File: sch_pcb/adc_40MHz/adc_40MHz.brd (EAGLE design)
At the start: 100 x 70 mm, 74 parts, among them IC1 AD9235BC, IC2 LT6600-15, IC3 LTC6254XMS, IC4 SN74LVC2G14DBV, IC5 LT1521XST, IC6 SN74LVC2G14DBV, X1 SMA-142-0701-851/861, X2 SMA-142-0701-851/861

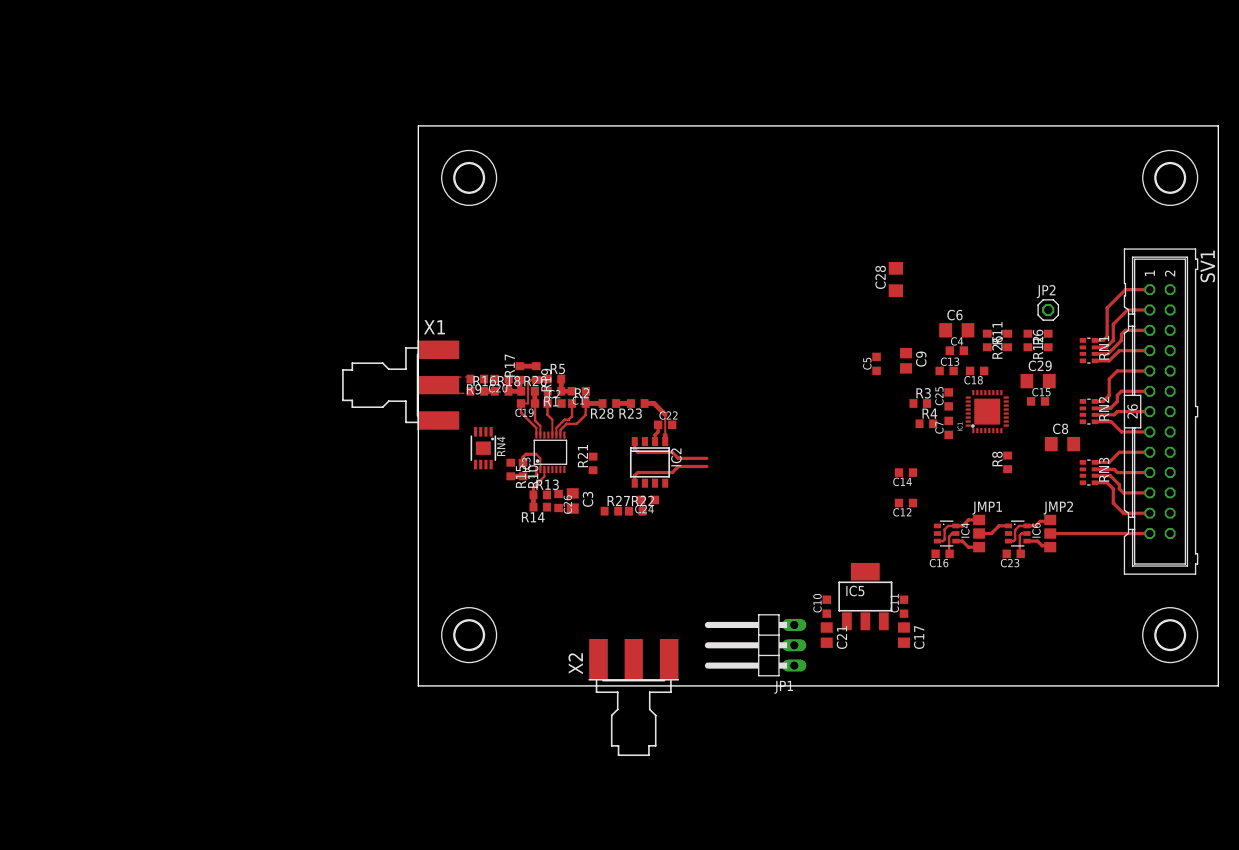
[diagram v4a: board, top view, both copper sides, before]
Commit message: Dodano rezystory ustalające stan buforów. Sygnały w filrach skończone
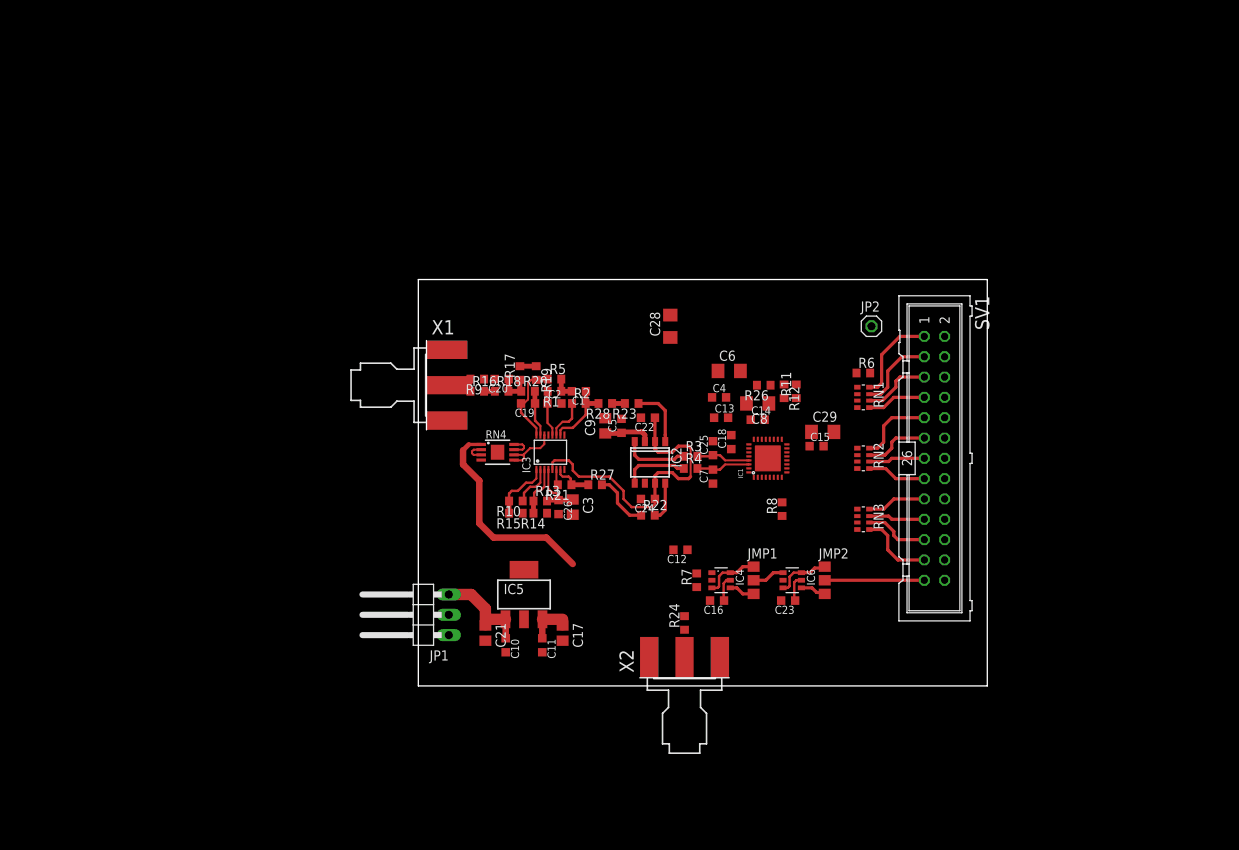
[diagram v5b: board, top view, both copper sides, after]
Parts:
- removed H1, H2, H3, H4: MOUNT-HOLE3.6, holes:3,6
- added R24: 0R, rcl:R0603
- added R7: 1M, rcl:R0603
- moved C11 45.5 mm to (15.5, 5.08), turned to 270 degrees
- moved JP1 43.3 mm to (0.00, 8.89)
- moved C17 42.7 mm to (18.0, 6.60)
- moved C21 42.7 mm to (8.38, 6.60)
- moved IC5 42.7 mm to (13.2, 11.4)
- moved C10 40.4 mm to (10.9, 5.08), turned to 270 degrees
- moved C9 38.5 mm to (23.4, 32.5), turned to 90 degrees
- moved C8 38.4 mm to (42.4, 35.3), turned to 180 degrees
- moved C5 32.8 mm to (25.4, 32.5)
- moved C18 32.0 mm to (39.1, 30.5), turned to 90 degrees
- moved R12 31.1 mm to (45.7, 36.8)
- moved C4 30.3 mm to (37.6, 36.1)
- moved C7 30.1 mm to (36.8, 26.2)
- moved C25 30.1 mm to (36.8, 29.7)
- moved R4 30.0 mm to (34.0, 27.2)
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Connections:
- new net N$18: R24.1, X2.1
- new net SIGIN: R16.1, R9.2, X1.1
- net GND: now also R7.1
- net N$34: now also R24.2, R7.2; no longer X2.1
- net VIN: no longer R16.1, R9.2, X1.1
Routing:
- net +3V3: track 6.51 -> 53.1 mm
- net N$10: track 2.26 -> 38.7 mm
- net VIN: track 0.00 -> 12.4 mm
- net N$24: track 0.00 -> 7.42 mm
- net N$42: track 0.00 -> 7.23 mm
- net N$3: track 0.00 -> 6.76 mm
- net N$2: track 0.00 -> 6.76 mm
- net N$13: track 0.00 -> 5.04 mm
- net N$30: track 0.00 -> 4.94 mm
- net SIGIN: track 0.00 -> 4.80 mm
- net N$15: track 3.95 -> 7.78 mm
- net N$16: track 0.00 -> 2.92 mm
- net N$25: track 0.00 -> 2.70 mm
- net N$1: track 10.4 -> 8.21 mm
- net N$4: track 10.4 -> 8.21 mm
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- removed copper zone on layer 1, net VIN
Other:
- board size 100 x 70 mm -> 71.1 x 50.8 mm

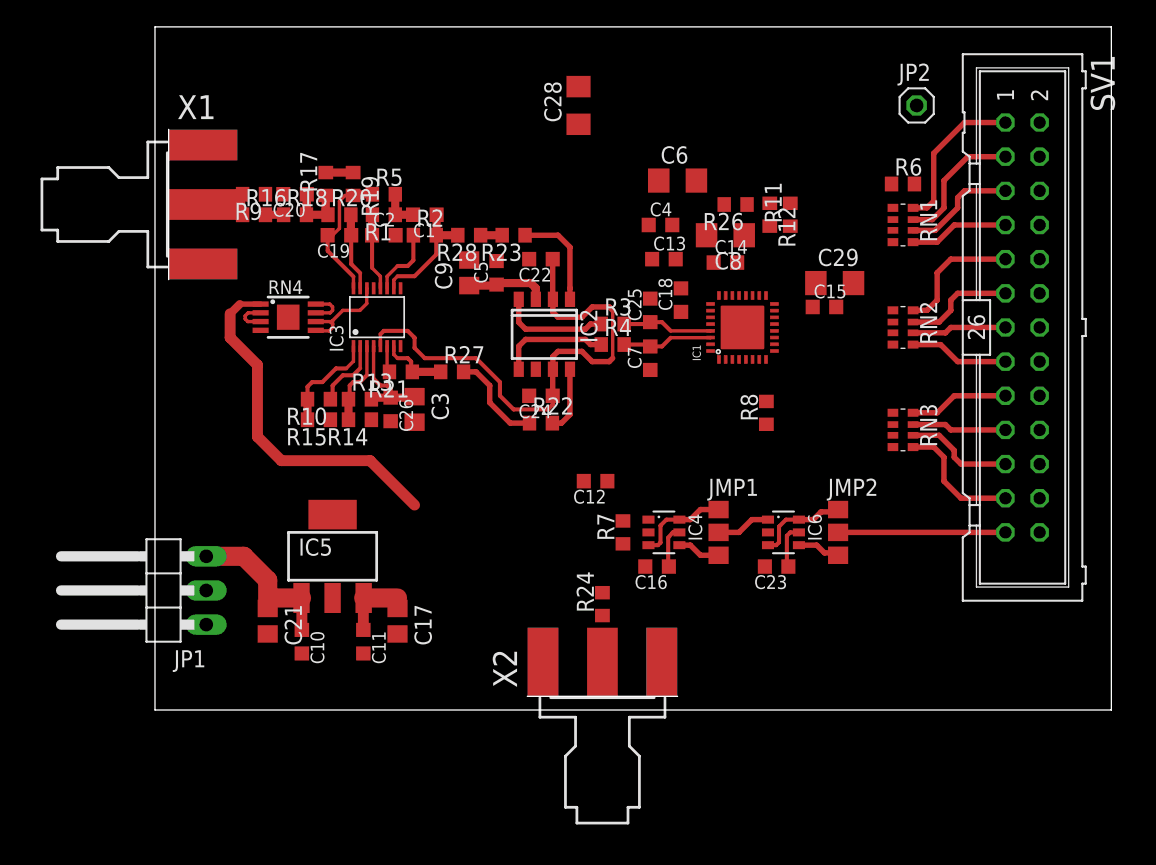
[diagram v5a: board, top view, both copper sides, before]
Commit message: Usunięto niepotrzebne rezystory, aby ułatwić projekt ścieżek. Gotowa płytka
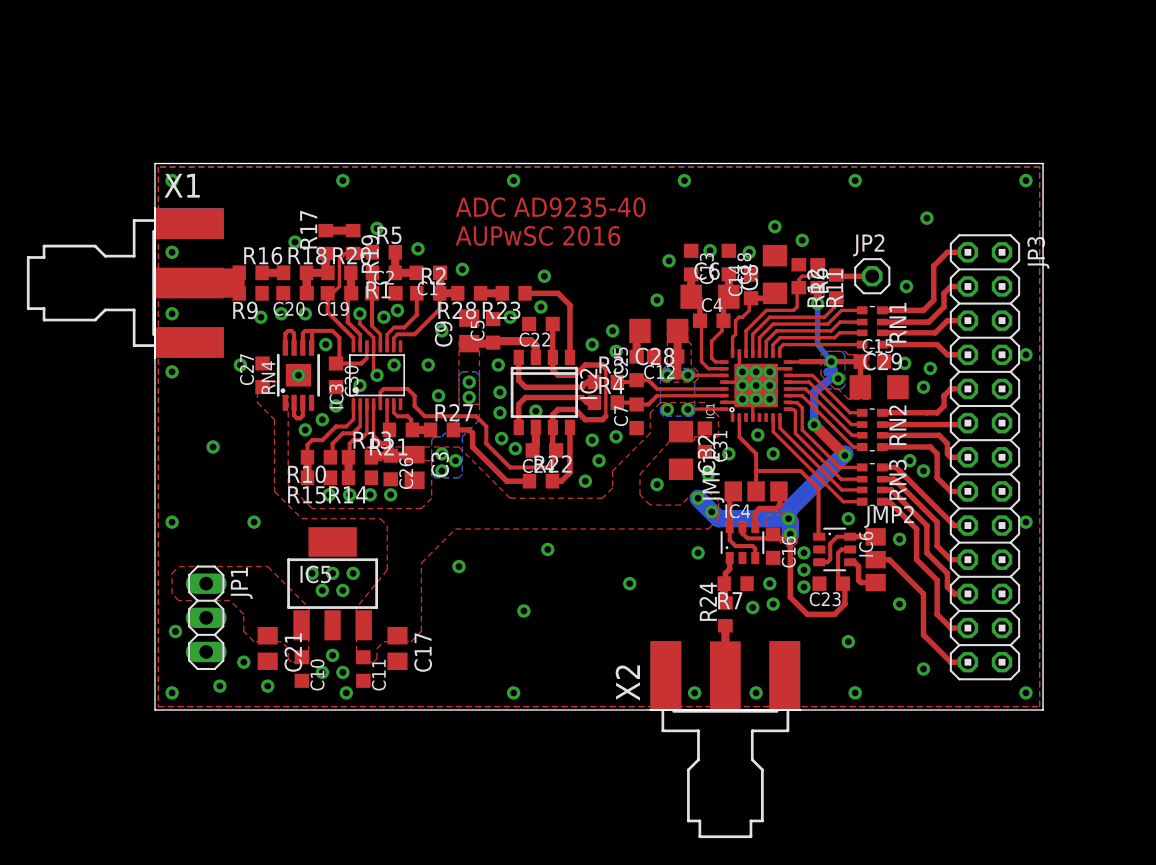
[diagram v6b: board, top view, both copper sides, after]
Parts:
- removed R26, R8: 0R, rcl:R0603
- removed SV1: (no value), con-harting-ml:ML26
- added C27, C30, C31: 100n, resistor:C0603K
- added C32: 10u, rcl:C1206
- added JP3: (no value), moj_pinhead:2X13
- JP1: device pinhead:1X03/90 -> moj_pinhead:1X03
- moved C28 17.8 mm to (37.5, 28.2), turned to 180 degrees
- moved JP2 13.1 mm to (53.3, 32.3)
- moved C12 10.6 mm to (38.0, 26.3)
- moved R7 9.21 mm to (43.2, 9.40), turned to 180 degrees
- moved X2 9.20 mm to (42.4, 0.00)
- moved R24 9.18 mm to (42.4, 7.11)
- moved R6 9.09 mm to (50.7, 31.5), turned to 90 degrees
- moved C6 8.97 mm to (41.3, 30.7)
- moved C16 8.77 mm to (46.0, 12.2), turned to 270 degrees
- moved C29 8.42 mm to (53.8, 24.0)
- moved C4 8.07 mm to (41.4, 29.0)
- moved RN2 7.96 mm to (53.3, 20.8)
- moved RN1 7.96 mm to (53.3, 28.4)
- moved R9 7.37 mm to (7.11, 31.0)
- moved C20 7.37 mm to (10.4, 31.0)
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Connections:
- removed net N$35: IC1.23, R26.2
- removed net N$9: IC1.4, R8.2
- net +3V3: now also C27.1, C31.1, C32.1
- net CLK: now also JP3.25; no longer SV1.25
- net DAC_D0: now also JP3.23; no longer SV1.23
- net DAC_D1: now also JP3.21; no longer SV1.21
- net DAC_D10: now also JP3.3; no longer SV1.3
- net DAC_D11: now also JP3.1; no longer SV1.1
- net DAC_D2: now also JP3.19; no longer SV1.19
- net DAC_D3: now also JP3.17; no longer SV1.17
- net DAC_D4: now also JP3.15; no longer SV1.15
- net DAC_D5: now also JP3.13; no longer SV1.13
- net DAC_D6: now also JP3.11; no longer SV1.11
- net DAC_D7: now also JP3.9; no longer SV1.9
- net DAC_D8: now also JP3.7; no longer SV1.7
- net DAC_D9: now also JP3.5; no longer SV1.5
- net GND: now also C27.2, C30.2, C31.2, C32.2, IC1.23, IC1.4, JP3.10, JP3.12, JP3.14, JP3.16, JP3.18, JP3.2, JP3.20, JP3.22, JP3.24, JP3.26, JP3.4, JP3.6, JP3.8; no longer R26.1, R8.1, SV1.10, SV1.12, SV1.14, SV1.16, SV1.18, SV1.2, SV1.20, SV1.22, SV1.24, SV1.26, SV1.4, SV1.6, SV1.8
- net N$24: now also C30.1
- net VIN: now also JP1.1; no longer JP1.3
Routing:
- net +3V3: track 53.1 -> 83.4 mm, vias 0 -> 18
- net GND: track 1.23 -> 16.9 mm, vias 0 -> 118
- net VIN: track 12.4 -> 0.04 mm
- net N$37: track 4.07 -> 14.8 mm
- net N$32: track 0.00 -> 10.5 mm
- net ADC_D0: track 0.00 -> 9.84 mm
- net ADC_D11: track 0.00 -> 9.66 mm
- net N$6: track 0.00 -> 9.10 mm
- net N$33: track 0.00 -> 8.97 mm
- net ADC_D1: track 0.00 -> 8.82 mm
- net ADC_D10: track 0.00 -> 8.64 mm
- net ADC_D2: track 0.00 -> 8.64 mm
- net ADC_D3: track 0.00 -> 8.48 mm
- net N$7: track 0.00 -> 8.30 mm
- net ADC_D9: track 0.00 -> 7.66 mm
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- added copper zone on layer 1, net +3V3
- added copper zone on layer 16, net +3V3
- added copper zone on layer 1, net GND
- added copper zone on layer 16, net GND
- added copper zone on layer 1, net VIN
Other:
- board size 71.1 x 50.8 mm -> 66 x 40.6 mm
- board text added: "ADC AD9235-40 AUPwSC 2016"

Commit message: Dodano przelotki dla wzmocnienia płytki przy złączach SMA
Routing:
- net GND: vias 118 -> 130
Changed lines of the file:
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@@
 <wire x1="35.814" y1="27.686" x2="36.068" y2="27.94" width="0.6096" layer="1"/>
 <via x="44.831" y="20.447" extent="1-16" drill="0.5" diameter="1"/>
+<via x="37.973" y="4.318" extent="1-16" drill="0.5" diameter="1"/>
+<via x="37.973" y="2.794" extent="1-16" drill="0.5" diameter="1"/>
+<via x="37.973" y="1.27" extent="1-16" drill="0.5" diameter="1"/>
+<via x="46.863" y="4.318" extent="1-16" drill="0.5" diameter="1"/>
+<via x="46.863" y="1.27" extent="1-16" drill="0.5" diameter="1"/>
+<via x="46.863" y="2.794" extent="1-16" drill="0.5" diameter="1"/>
+<via x="1.27" y="36.195" extent="1-16" drill="0.5" diameter="1"/>
+<via x="4.318" y="36.195" extent="1-16" drill="0.5" diameter="1"/>
+<via x="2.794" y="36.195" extent="1-16" drill="0.5" diameter="1"/>
+<via x="1.27" y="27.305" extent="1-16" drill="0.5" diameter="1"/>
+<via x="4.318" y="27.305" extent="1-16" drill="0.5" diameter="1"/>
+<via x="2.794" y="27.305" extent="1-16" drill="0.5" diameter="1"/>
 </signal>
 <signal name="N$1">

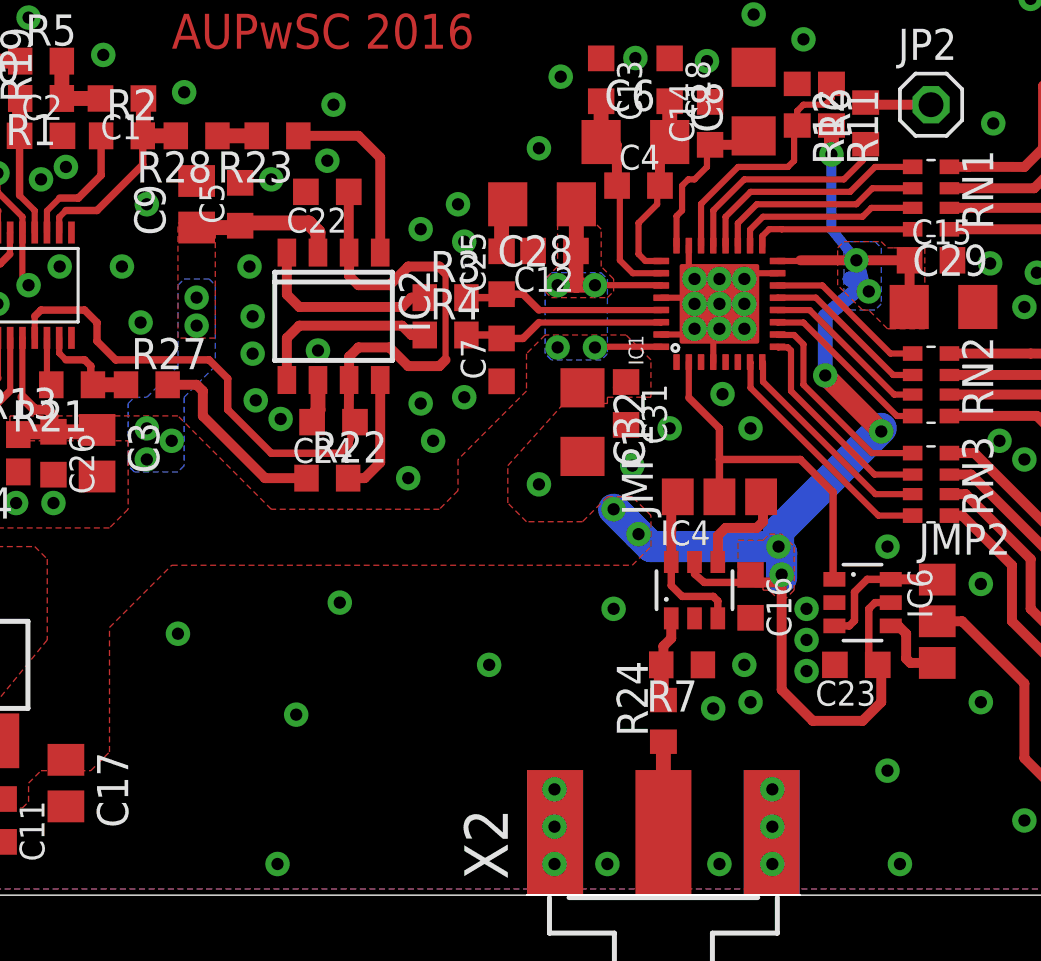
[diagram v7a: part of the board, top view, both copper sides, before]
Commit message: Niewielkie poprawki - dodano połączenie masy przy ADC
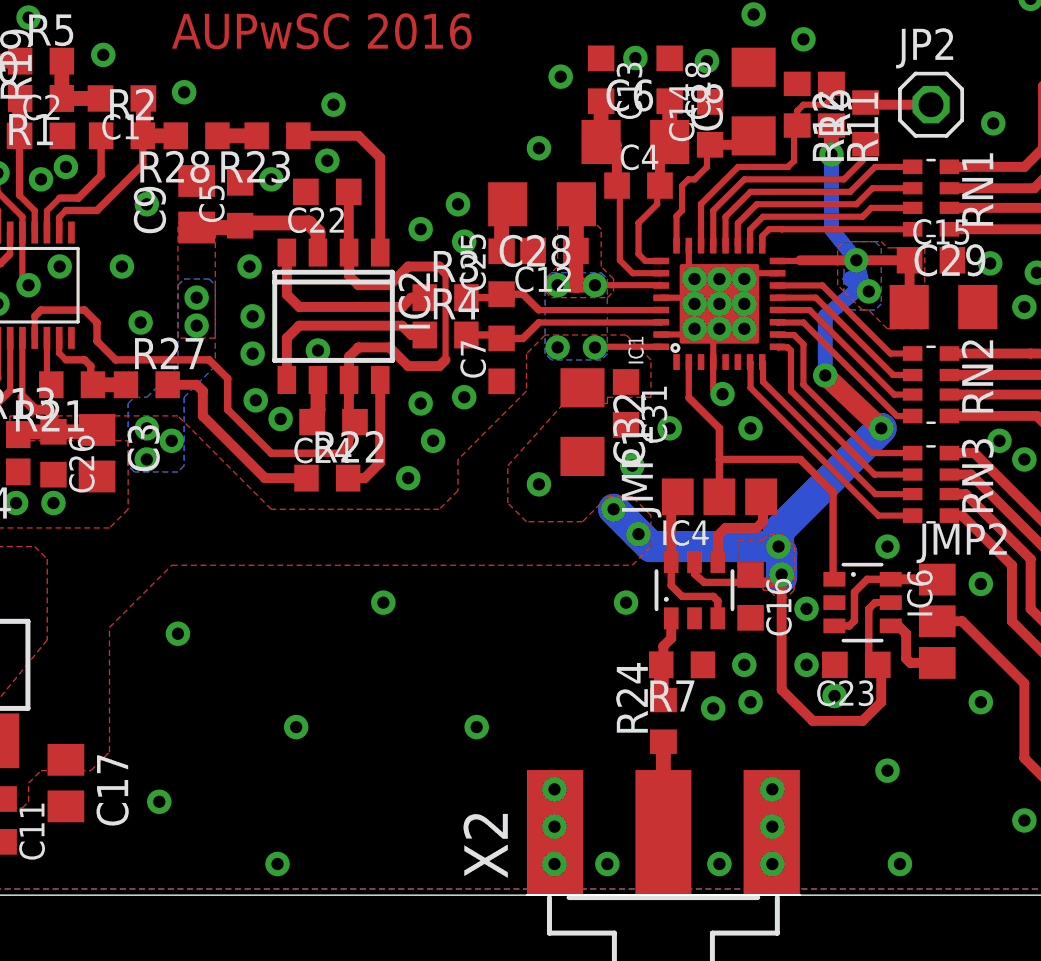
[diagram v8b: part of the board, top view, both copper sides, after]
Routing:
- net GND: track 16.9 -> 18.2 mm, vias 130 -> 131
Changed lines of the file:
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@@
 <layer number="45" name="Holes" color="7" fill="1" visible="no" active="yes"/>
 <layer number="46" name="Milling" color="3" fill="1" visible="no" active="yes"/>
-<layer number="47" name="Measures" color="7" fill="1" visible="no" active="yes"/>
+<layer number="47" name="Measures" color="7" fill="1" visible="yes" active="yes"/>
 <layer number="48" name="Document" color="7" fill="1" visible="yes" active="yes"/>
 <layer number="49" name="Reference" color="7" fill="1" visible="yes" active="yes"/>
@@
 <text x="22.352" y="34.544" size="1.4224" layer="1" ratio="20">ADC AD9235-40
 AUPwSC 2016</text>
+<dimension x1="0" y1="40.64" x2="66.04" y2="40.64" x3="33.02" y3="42.672" textsize="1.778" layer="47"/>
+<dimension x1="66.04" y1="40.64" x2="66.04" y2="0" x3="70.612" y3="20.32" textsize="1.778" layer="47"/>
 </plain>
 <attributes>
@@
 <via x="57.15" y="24.003" extent="1-16" drill="0.5" diameter="1"/>
 <via x="48.26" y="11.684" extent="1-16" drill="0.5" diameter="1"/>
-<via x="48.26" y="10.414" extent="1-16" drill="0.5" diameter="1"/>
-<via x="48.26" y="9.144" extent="1-16" drill="0.5" diameter="1"/>
+<via x="48.26" y="9.398" extent="1-16" drill="0.5" diameter="1"/>
+<via x="49.403" y="8.128" extent="1-16" drill="0.5" diameter="1"/>
 <via x="45.72" y="9.398" extent="1-16" drill="0.5" diameter="1"/>
 <via x="44.45" y="7.62" extent="1-16" drill="0.5" diameter="1"/>
@@
 <via x="28.702" y="29.972" extent="1-16" drill="0.5" diameter="1"/>
 <via x="22.606" y="10.668" extent="1-16" drill="0.5" diameter="1"/>
-<via x="29.21" y="11.938" extent="1-16" drill="0.5" diameter="1"/>
-<via x="40.386" y="11.684" extent="1-16" drill="0.5" diameter="1"/>
-<via x="35.306" y="9.398" extent="1-16" drill="0.5" diameter="1"/>
-<via x="27.432" y="7.366" extent="1-16" drill="0.5" diameter="1"/>
+<via x="30.988" y="11.938" extent="1-16" drill="0.5" diameter="1"/>
+<via x="40.894" y="11.938" extent="1-16" drill="0.5" diameter="1"/>
+<via x="34.798" y="6.858" extent="1-16" drill="0.5" diameter="1"/>
+<via x="27.432" y="6.858" extent="1-16" drill="0.5" diameter="1"/>
 <wire x1="35.814" y1="26.416" x2="35.814" y2="27.686" width="0.6096" layer="1"/>
 <wire x1="35.814" y1="27.686" x2="36.068" y2="27.94" width="0.6096" layer="1"/>
@@
 <via x="4.318" y="27.305" extent="1-16" drill="0.5" diameter="1"/>
 <via x="2.794" y="27.305" extent="1-16" drill="0.5" diameter="1"/>
+<wire x1="44.45" y1="21.844" x2="44.45" y2="20.574" width="0.254" layer="1"/>
+<via x="21.844" y="3.81" extent="1-16" drill="0.5" diameter="1"/>
 </signal>
 <signal name="N$1">
@@
 <via x="49.276" y="30.226" extent="1-16" drill="0.5" diameter="1"/>
 <via x="50.292" y="25.908" extent="1-16" drill="0.5" diameter="1"/>
-<wire x1="49.276" y1="30.226" x2="49.276" y2="27.178" width="0.4064" layer="16"/>
-<wire x1="49.276" y1="27.178" x2="50.292" y2="25.908" width="0.4064" layer="16"/>
+<wire x1="49.276" y1="30.226" x2="49.276" y2="27.178" width="0.6096" layer="16"/>
+<wire x1="49.276" y1="27.178" x2="50.292" y2="25.908" width="0.6096" layer="16"/>
 <wire x1="51.696" y1="11.938" x2="51.054" y2="11.938" width="0.3048" layer="1"/>
 <wire x1="51.054" y1="11.938" x2="50.8" y2="11.684" width="0.3048" layer="1"/>
@@
 </polygon>
 <via x="49.022" y="21.209" extent="1-16" drill="0.5" diameter="1"/>
-<via x="51.308" y="18.923" extent="1-16" drill="0.5" diameter="1"/>
-<wire x1="49.022" y1="21.209" x2="51.308" y2="18.923" width="0.8128" layer="1"/>
+<via x="51.308" y="19.05" extent="1-16" drill="0.5" diameter="1"/>
+<wire x1="49.022" y1="21.209" x2="51.308" y2="19.05" width="0.8128" layer="1"/>
 <wire x1="40.386" y1="15.748" x2="41.402" y2="14.732" width="1.27" layer="16"/>
 <wire x1="41.402" y1="14.732" x2="41.91" y2="14.224" width="1.27" layer="16"/>
@@
 <wire x1="47.978" y1="25.88" x2="48.006" y2="25.908" width="0.254" layer="1"/>
 <wire x1="48.006" y1="25.908" x2="50.292" y2="25.908" width="0.4064" layer="1"/>
-<wire x1="51.308" y1="19.05" x2="51.308" y2="18.923" width="0" layer="19" extent="16-16"/>
 <wire x1="47.244" y1="12.954" x2="47.244" y2="13.081" width="0" layer="19" extent="16-16"/>
 </signal>
